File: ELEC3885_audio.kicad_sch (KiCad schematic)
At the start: 43 parts, among them J1 MicInstIn, J2 LineIn, J3 HeadPhoneOut, J4 LineOutR, J5 LineOutL, J9 Conn_01x05_Female, U1 AP7313, U2 SGTL5000XNLA3, U8 NE5532

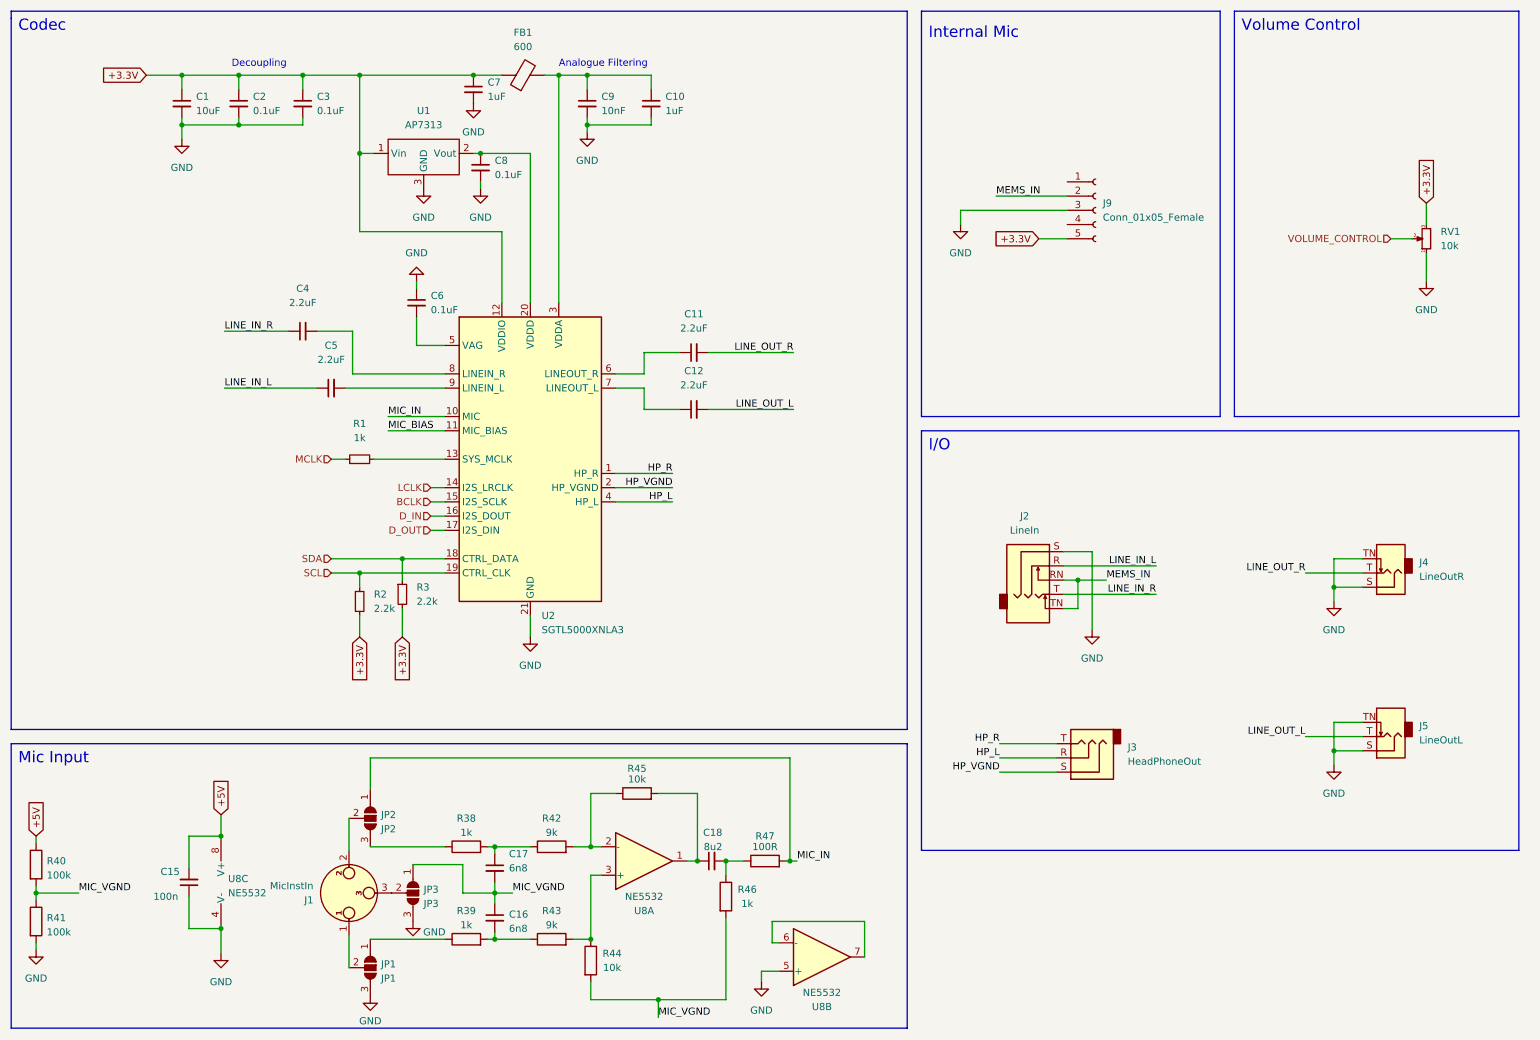
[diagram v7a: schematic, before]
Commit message: Encoders, RGB LED added, PCB cleanup
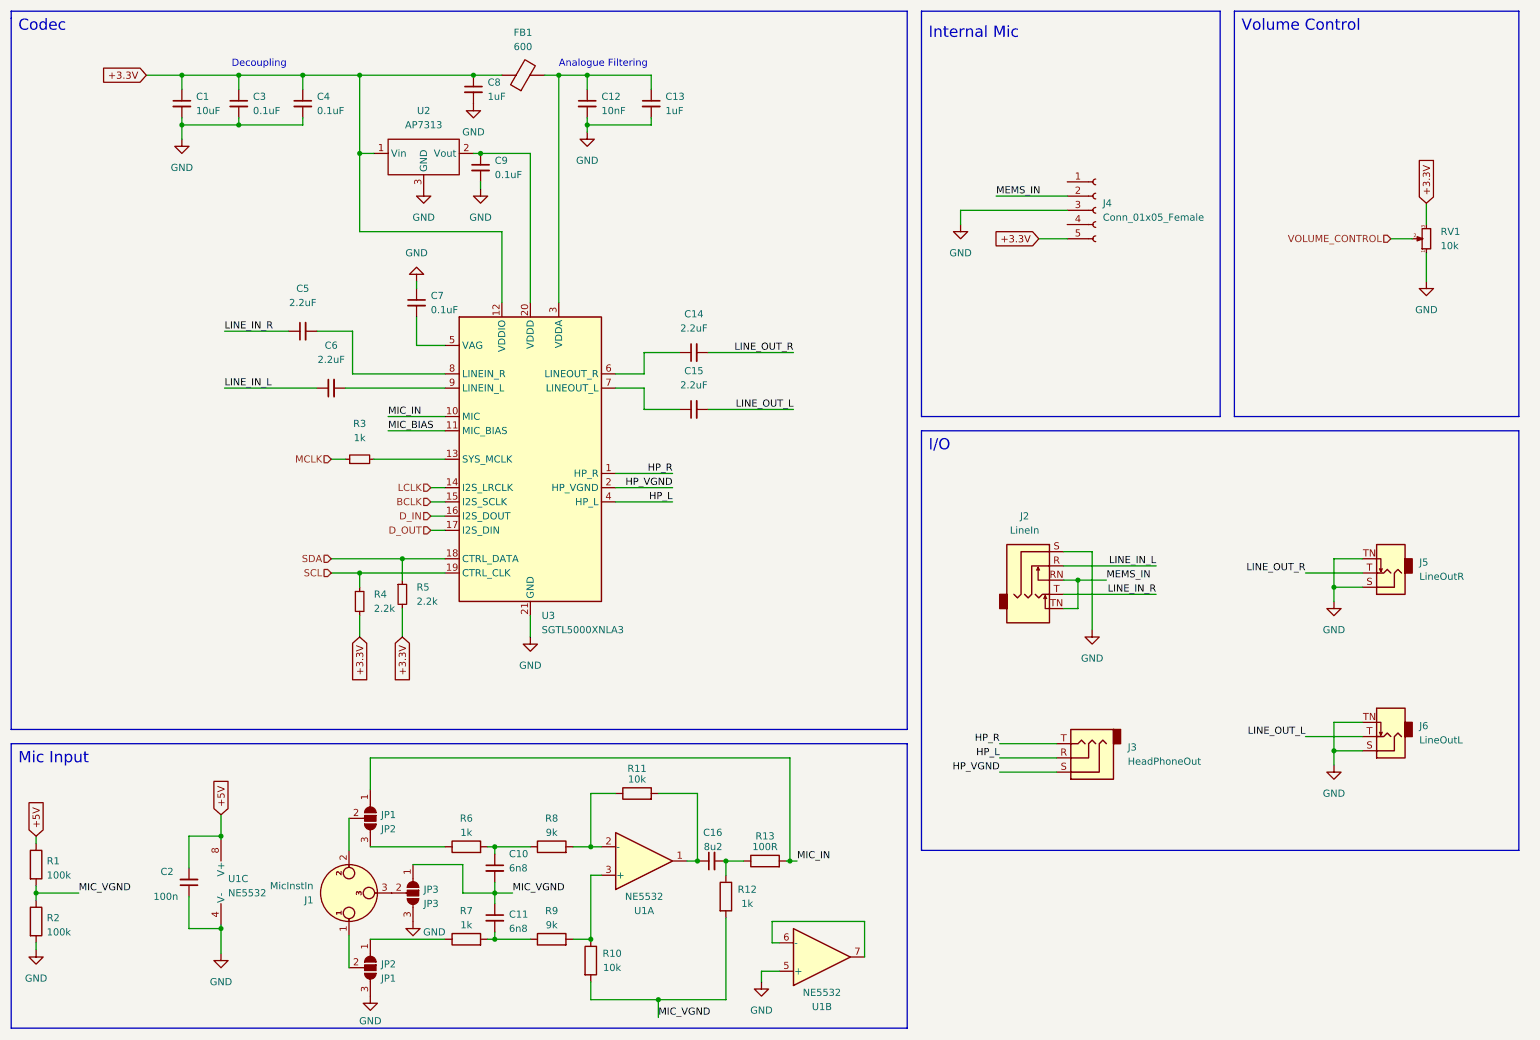
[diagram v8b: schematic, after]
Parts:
- renumbered C17 to C10, C16 to C11, C9 to C12, C10 to C13, C11 to C14, C12 to C15, C18 to C16, C15 to C2, C2 to C3, C3 to C4, C4 to C5, C5 to C6, C6 to C7, C7 to C8, C8 to C9, J9 to J4, J4 to J5, J5 to J6, JP2 to JP1, JP1 to JP2, R40 to R1, R44 to R10, R45 to R11, R46 to R12, R47 to R13, R41 to R2, R1 to R3, R2 to R4, R3 to R5, R38 to R6, R39 to R7, R42 to R8, R43 to R9, U8 to U1, U1 to U2, U2 to U3
